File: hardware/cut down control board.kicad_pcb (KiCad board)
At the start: 2 copper layers, 152.4 x 63.7 mm, 49 parts, among them J1 CUTTER, J10 SAT(10 picoblade), J11 VGPS SELECT, J12 Analog In, J2 MOTOR, J3 ISP, J5 SAT(PIN HDR), J6 GPS(PIN HDR), J7 DBG TTL, J9 GPS(JST SH)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

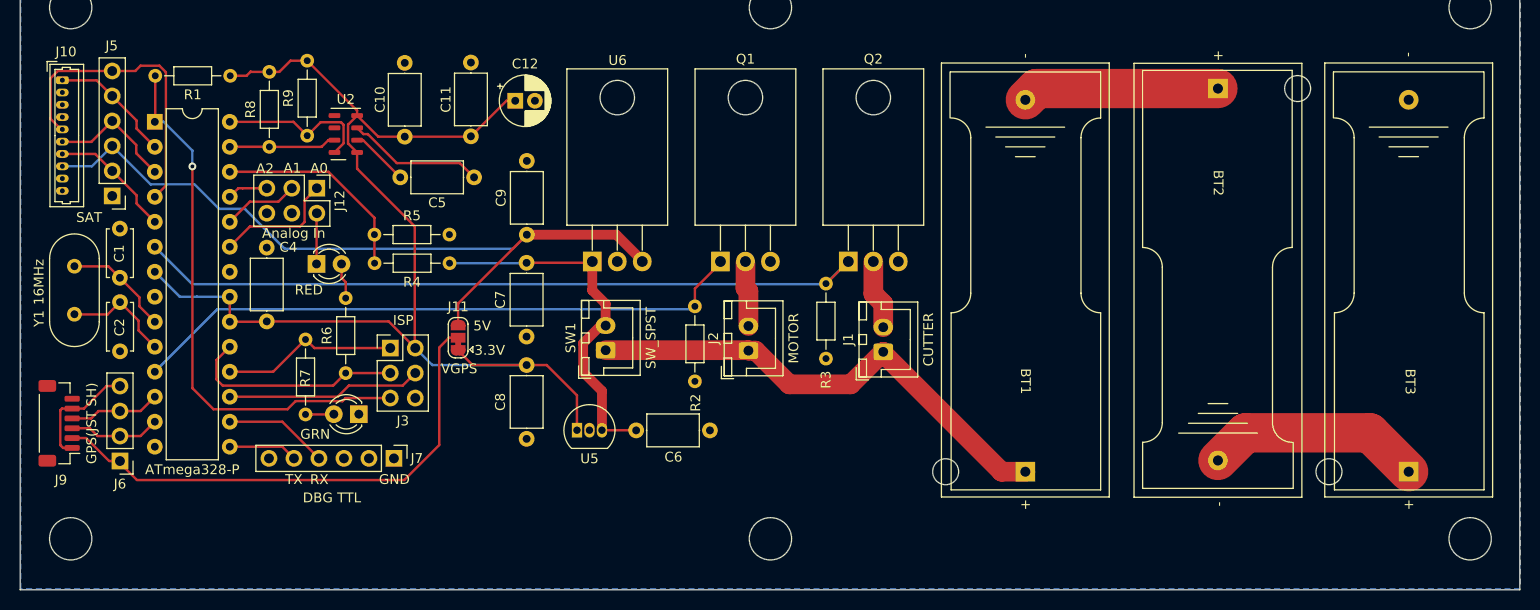
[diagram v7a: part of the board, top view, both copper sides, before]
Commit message: Added graphics, D8 input, and external power connector
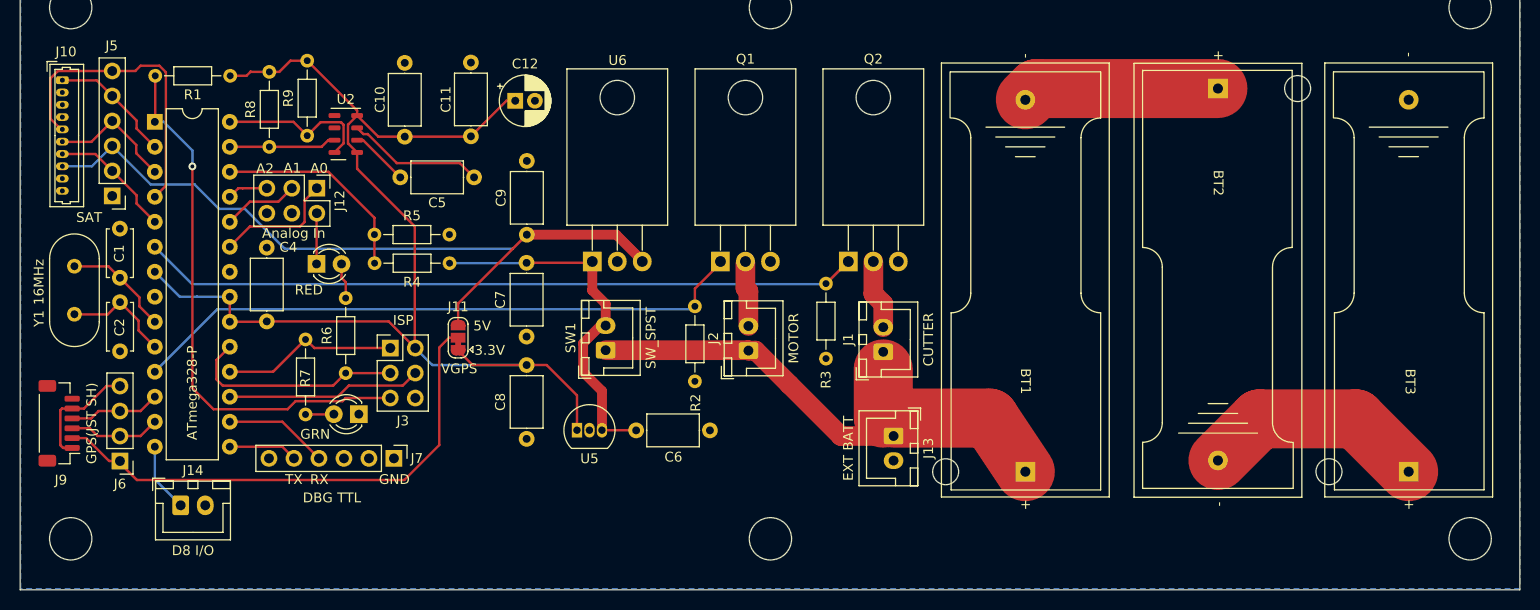
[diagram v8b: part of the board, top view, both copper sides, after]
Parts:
- added G***: LOGO, LOGO, B.Cu at (210.3, 100.9)
- added J13: EXT BATT, Connector_JST:JST_XH_B2B-XH-A_1x02_P2.50mm_Vertical, F.Cu at (164.4, 115.8)
- added J14: D8 I/O, Connector_JST:JST_XH_B2B-XH-A_1x02_P2.50mm_Vertical, F.Cu at (91.9, 122.9)
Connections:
- U1 pad 14: unconnected-(U1-Pad14) -> Net-(U1-Pad14)
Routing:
- net Net-(U1-Pad14): track 0.00 -> 7.05 mm
- net VDD: track 50.8 -> 56.0 mm
- net Net-(BT2-Pad2): track 22.2 -> 23.4 mm
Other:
- board text added: "ATOMIC WOMBAT"
- board text added: "SETTINGS"
- board text added: "https://github.com/dwkennedy/ballooning VERSION 10/11/2022"
- board text removed: "https://github.com/dwkennedy/ballooning 10/11/2022"
